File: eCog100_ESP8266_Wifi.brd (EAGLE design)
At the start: 48 x 28 mm, 1 part

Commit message: V1.1
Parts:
- added R1, R2, R3, R4: 10K, GadgetFactory:0805
- added X1: (no value), adafruit:ESP-12
- ECOG: value ECOG_BUSES_ROWECOG_BUSES_SMD -> ECOG_GENERAL_ROWECOG_GENERAL_SMD; device eCogs:ECOG_BUSES_SMD -> eCogs:ECOG_GENERAL_SMD
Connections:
- new net GPIO0/BOOTLOAD: ECOG.3, X1.12
- new net N$3: R1.1, X1.11
- new net N$4: R2.2, X1.10
- new net N$5: R4.1, X1.3
- new net RESET: ECOG.4, R3.1, X1.1, X1.4
- new net RX: ECOG.2, X1.15
- new net TX: ECOG.1, X1.16
- net 3V3: now also R1.2, R3.2, R4.2, X1.8
- net GND: now also R2.1, X1.9
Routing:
- net 3V3: track 3.55 -> 56.7 mm, vias 1 -> 2
- net RESET: track 0.00 -> 49.1 mm
- net RX: track 0.00 -> 29.1 mm
- net TX: track 0.00 -> 28.6 mm
- net GPIO0/BOOTLOAD: track 0.00 -> 19.1 mm
- net N$5: track 0.00 -> 3.63 mm
- net N$4: track 0.00 -> 2.90 mm
- net N$3: track 0.00 -> 2.56 mm
- added copper zone on layer 1, net GND
- removed copper zone on layer 1, net 3V3
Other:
- board text added: "ESP8266 WIFI"
- board text added: "GPIO0/Bootload"
- board text added: "RX>"
- board text added: "TX<"
- board text removed: "5V"
- board text removed: "I2C-SCL"
- board text removed: "I2C-SDA"
- board text removed: "P5<>"
- board text removed: "Project Name"
- board text removed: "SPI-CS>"
- board text removed: "SPI-MOSI<"
- board text removed: "SPI-MOSI>"
- board text removed: "SPI-SCK>"

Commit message: Latest updated to V1.4
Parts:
- added U$1: (no value), GadgetFactory:GADGETBOX_TEXT
- added U$2, U$3, U$4, U$5: (no value), eCogs:LEGEND_DIO
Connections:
- net GPIO0/BOOTLOAD: now also ECOG.G2; no longer ECOG.3
- net RESET: now also ECOG.G3; no longer ECOG.4
- net RX: now also ECOG.G1; no longer ECOG.2
- net TX: now also ECOG.G0; no longer ECOG.1
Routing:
- net RESET: track 49.1 -> 37.3 mm
- net RX: track 29.1 -> 31.6 mm
- net 3V3: track 56.7 -> 59.1 mm
- net TX: track 28.6 -> 29.6 mm
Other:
- board text added: "GPIO0 Bootload"
- board text added: "ecog100 v1.1"
- board text removed: "GPIO0/Bootload"
- board text removed: "ecog100 v1.0"

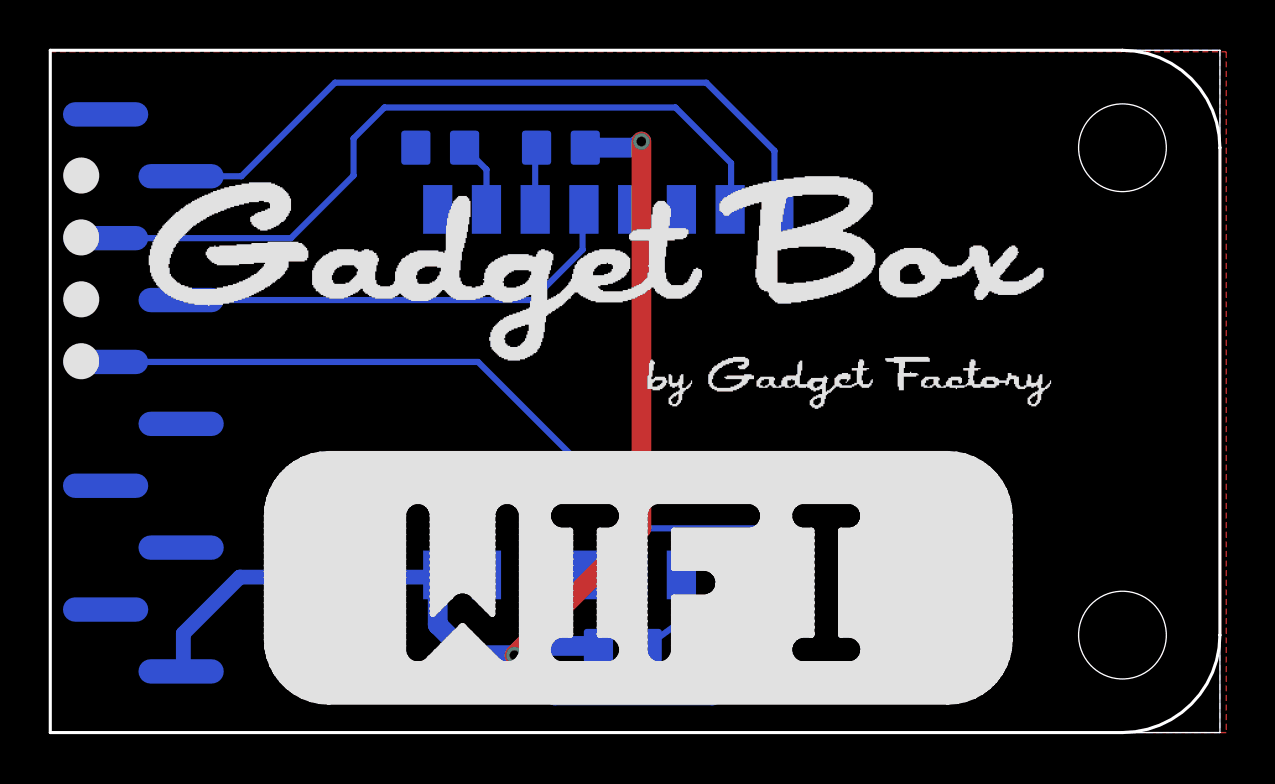
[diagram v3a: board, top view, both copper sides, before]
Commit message: Added Box text to silkscreen
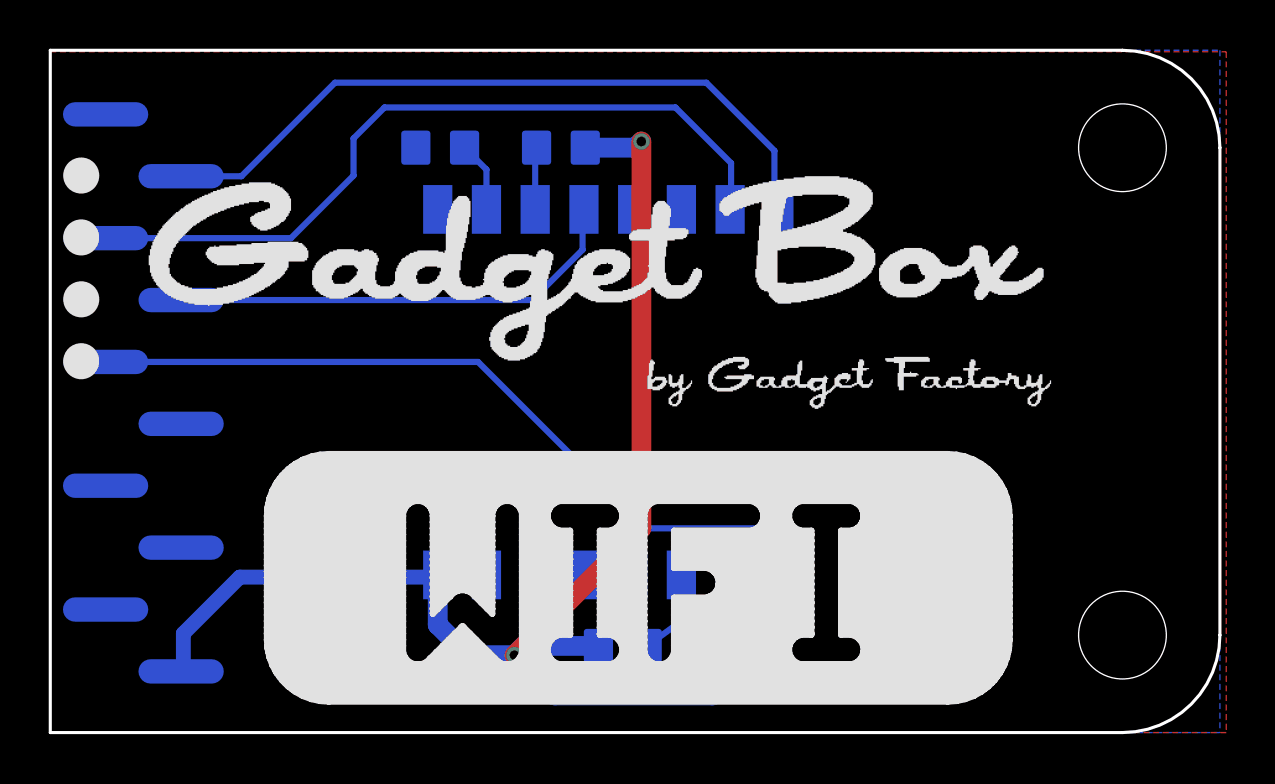
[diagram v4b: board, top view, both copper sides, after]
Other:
- outline, holes or cut-outs redrawn
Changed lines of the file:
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@@
 <board>
 <plain>
-<wire x1="0" y1="0" x2="48" y2="0" width="0" layer="20"/>
-<wire x1="48" y1="0" x2="48" y2="28" width="0" layer="20"/>
-<wire x1="48" y1="28" x2="0" y2="28" width="0" layer="20"/>
-<wire x1="0" y1="28" x2="0" y2="0" width="0" layer="20"/>
 <text x="40.767" y="23.368" size="0.8128" layer="22" font="vector" rot="MR270">ecog100.GadgetFactory.net</text>
 <text x="41.402" y="1.016" size="1.016" layer="22" font="vector" rot="MR0">ecog100 v1.1</text>

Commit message: Update all of the Fonts and graphics
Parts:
- added U$6: (no value), ohw-logo:OSHW_FILLX200_NOTEXT
- moved U$1 1.77 mm to (24.5, 18.4)

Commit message: All the 2.0 updates
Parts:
- moved ECOG 55.8 mm to (48.3, 27.9), turned to 180 degrees
- moved R3 24.7 mm to (15.6, 24.4), turned to 180 degrees
- moved R2 23.6 mm to (28.4, 3.94), turned to 0 degrees
- moved U$6 23.0 mm to (21.0, 20.7)
- moved R4 21.0 mm to (21.0, 24.4), turned to 180 degrees
- moved R1 20.2 mm to (23.5, 3.94), turned to 0 degrees
- moved U$2 7.62 mm to (1.27, 15.2), turned to 180 degrees
- moved U$5 7.62 mm to (1.27, 22.9), turned to 180 degrees
- moved X1 6.35 mm to (19.1, 14.0), turned to 270 degrees
- moved U$3 2.54 mm to (1.27, 17.8), turned to 180 degrees
- moved U$4 2.54 mm to (1.27, 20.3), turned to 180 degrees
- moved U$1 2.04 mm to (24.6, 16.4)
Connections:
- net RX renamed RX/MOSI
- net TX renamed TX/MISO
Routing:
- net RESET: track 37.3 -> 30.9 mm
- net RX/MOSI: track 31.6 -> 25.9 mm, vias 0 -> 2
- net 3V3: track 59.1 -> 64.8 mm, vias 2 -> 3
- net GPIO0/BOOTLOAD: track 19.0 -> 22.9 mm
- net TX/MISO: track 29.6 -> 33.3 mm, vias 0 -> 2
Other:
- board size 48 x 28 mm -> 47.5 x 28 mm
- board text added: "0"
- board text added: "1"
- board text added: "2"
- board text added: "3"
- board text added: "RX/MOSI"
- board text added: "TX/MISO"
- board text added: "ecog100 v2.0"
- board text removed: "RX>"
- board text removed: "TX<"
- board text removed: "ecog100 v1.1"
